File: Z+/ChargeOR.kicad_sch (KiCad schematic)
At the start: 8 parts, among them U1 SI3865DDV-T1-GE3, U2 LTC4376CDHD_PBF

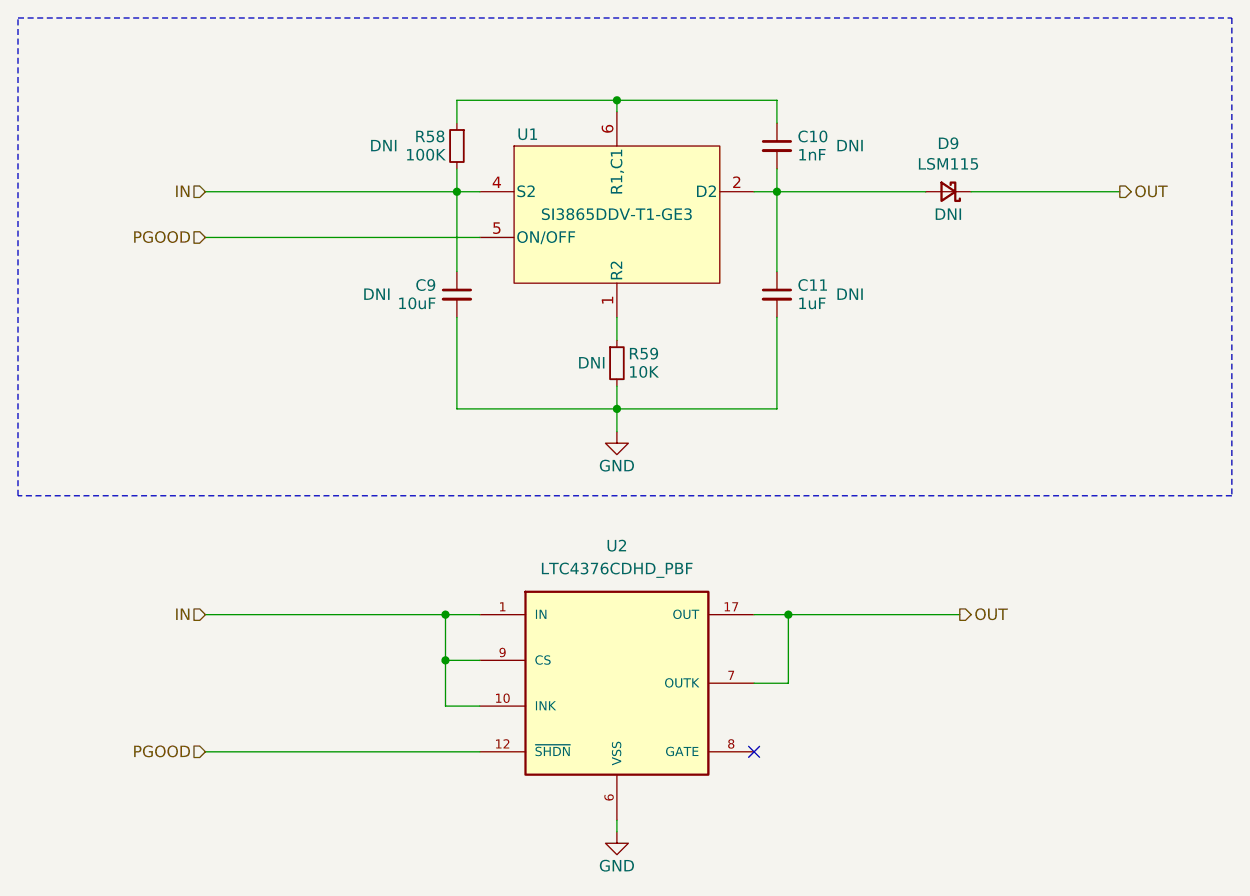
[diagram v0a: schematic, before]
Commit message: Added DRV8235, Quad Light Sensor, and refactored schematics
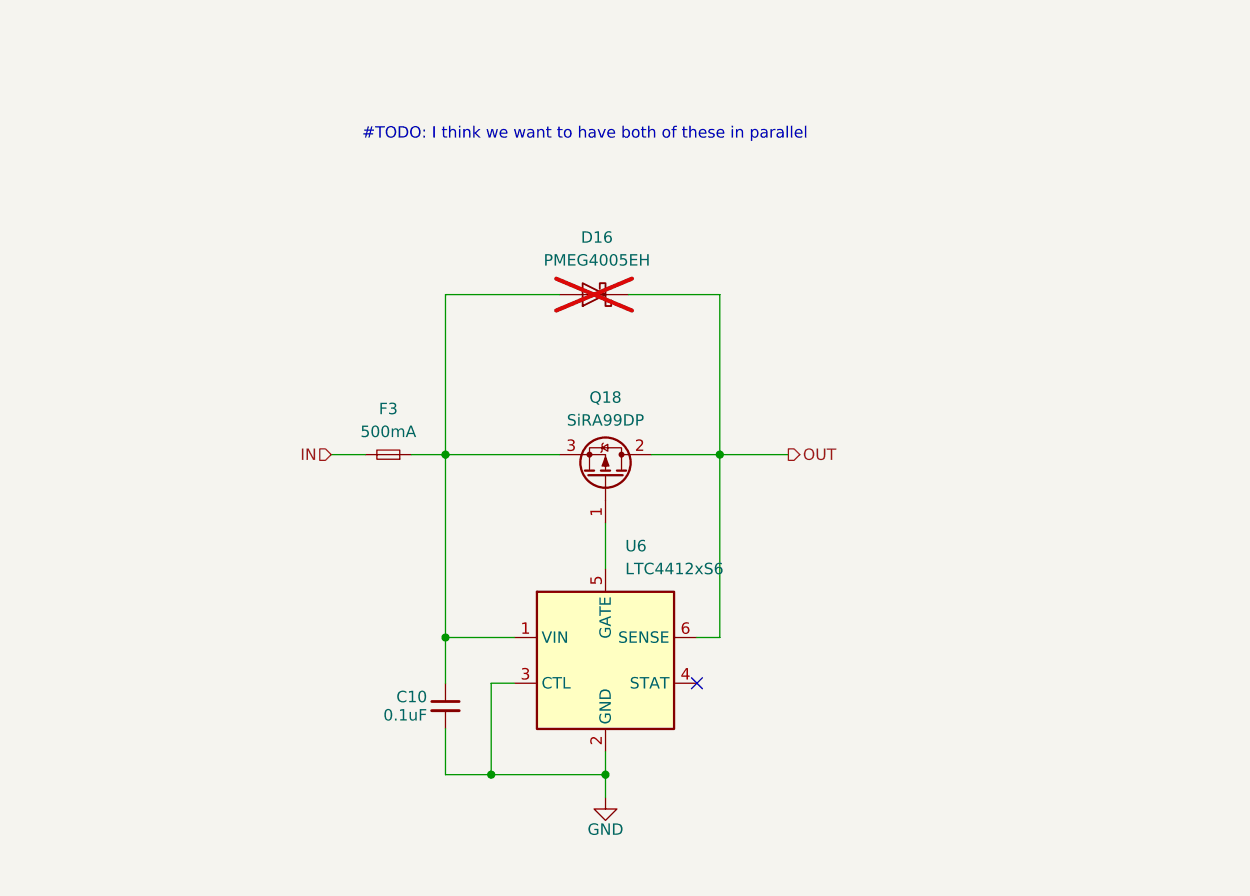
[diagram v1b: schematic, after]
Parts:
- removed C11: 1uF, Capacitor_SMD:C_1206_3216Metric, symbol Device:C_Small
- removed C9: 10uF, Capacitor_SMD:C_1206_3216Metric, symbol Device:C_Small
- removed D9: LSM115, SolarPanels:DO-214BA_MCH, symbol Device:D_Schottky_Small
- removed R58: 100K, Resistor_SMD:R_0603_1608Metric, symbol Device:R_Small
- removed R59: 10K, Resistor_SMD:R_0603_1608Metric, symbol Device:R_Small
- removed U1: SI3865DDV-T1-GE3, Package_TO_SOT_SMD:SOT-23-6, symbol SolarPanels:SI3865DDV-T1-GE3
- removed U2: LTC4376CDHD_PBF, Package_DFN_QFN:DFN-16-1EP_4x5mm_P0.5mm_EP2.44x4.34mm, symbol SolarPanels:LTC4376CDHD_PBF
- added D16: PMEG4005EH, Diode_SMD:D_SOD-123F, symbol Diode:PMEG4005EH
- added F3: 500mA, Fuse:Fuse_0603_1608Metric, symbol Device:Fuse_Small
- added Q18: SiRA99DP, Argus-Miscellaneous:PowerPAK SO-8, symbol Argus-IC:Q_PMOS_GDS
- added U6: LTC4412xS6, Package_TO_SOT_SMD:TSOT-23-6, symbol Power_Management:LTC4412xS6
- C10: value 1nF -> 0.1uF; DNI DNI -> (none)
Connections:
- net GND: now also C10.2, U6.2 (GND), U6.3 (CTL)
- net IN: now also F3.2
- net OUT: now also D16.1 (K), Q18.2 (D), U6.6 (SENSE)
- net at C10.1: now also D16.2 (A), F3.1, Q18.3 (S), U6.1 (VIN)
- new net: Q18.1 (G), U6.5 (GATE)
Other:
- note added: "#TODO: I think we want to have both of these in parallel"

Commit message: Z+ updates WIP
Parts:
- renumbered D16 to D2, F3 to F5, Q18 to Q7
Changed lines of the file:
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@@
 		(dnp yes)
 		(fields_autoplaced yes)
-		(property "Reference" "D16"
+		(property "Reference" "D2"
 			(at 145.0975 66.04 0)
 			(effects
@@
 			(project "Z+"
 				(path "/977a45af-b6d4-4b54-8e70-e74e2c44e8e7/3495d2a7-7425-4e27-a34a-beb5018fad2a/540f2f39-cb77-4d16-82f8-b8dbe6775262"
-					(reference "D16")
+					(reference "D2")
 					(unit 1)
 				)
@@
 		(dnp no)
 		(fields_autoplaced yes)
-		(property "Reference" "F3"
+		(property "Reference" "F5"
 			(at 121.92 85.09 0)
 			(effects
@@
 			(project "Z+"
 				(path "/977a45af-b6d4-4b54-8e70-e74e2c44e8e7/3495d2a7-7425-4e27-a34a-beb5018fad2a/540f2f39-cb77-4d16-82f8-b8dbe6775262"
-					(reference "F3")
+					(reference "F5")
 					(unit 1)
 				)
@@
 		(on_board yes)
 		(dnp no)
-		(property "Reference" "#PWR046"
+		(property "Reference" "#PWR021"
 			(at 146.05 134.62 0)
 			(effects
@@
 			(project "Z+"
 				(path "/977a45af-b6d4-4b54-8e70-e74e2c44e8e7/3495d2a7-7425-4e27-a34a-beb5018fad2a/540f2f39-cb77-4d16-82f8-b8dbe6775262"
-					(reference "#PWR046")
+					(reference "#PWR021")
 					(unit 1)
 				)
@@
 		(on_board yes)
 		(dnp no)
-		(property "Reference" "Q18"
+		(property "Reference" "Q7"
 			(at 146.05 83.82 90)
 			(effects
@@
 			(project "Z+"
 				(path "/977a45af-b6d4-4b54-8e70-e74e2c44e8e7/3495d2a7-7425-4e27-a34a-beb5018fad2a/540f2f39-cb77-4d16-82f8-b8dbe6775262"
-					(reference "Q18")
-					(unit 1)
-				)
+					(reference "Q7")
+					(unit 1)
+				)
